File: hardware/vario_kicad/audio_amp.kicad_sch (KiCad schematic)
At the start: 14 parts

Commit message: update footprints, add LSE oscillator
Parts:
- R16, R17, R18, R19, R20, R21: footprint (none) -> Resistor_SMD:R_0402_1005Metric
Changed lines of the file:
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@@
 			)
 		)
-		(property "Footprint" ""
+		(property "Footprint" "Resistor_SMD:R_0402_1005Metric"
 			(at 194.31 81.788 90)
 			(effects
@@
 			)
 		)
-		(property "Footprint" ""
+		(property "Footprint" "Resistor_SMD:R_0402_1005Metric"
 			(at 220.98 95.758 90)
 			(effects
@@
 			)
 		)
-		(property "Footprint" ""
+		(property "Footprint" "Resistor_SMD:R_0402_1005Metric"
 			(at 110.49 76.708 90)
 			(effects
@@
 			)
 		)
-		(property "Footprint" ""
+		(property "Footprint" "Resistor_SMD:R_0402_1005Metric"
 			(at 194.31 95.758 90)
 			(effects
@@
 			)
 		)
-		(property "Footprint" ""
+		(property "Footprint" "Resistor_SMD:R_0402_1005Metric"
 			(at 162.56 103.378 90)
 			(effects
@@
 			)
 		)
-		(property "Footprint" ""
+		(property "Footprint" "Resistor_SMD:R_0402_1005Metric"
 			(at 162.56 89.408 90)
 			(effects

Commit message: start layout
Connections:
- net GND: now also U1.9 (GNDPAD)
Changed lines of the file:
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@@
+	)
+	(junction
+		(at 121.92 111.76)
+		(diameter 0)
+		(color 0 0 0 0)
 	)
 	(junction
@@
 	(wire
 		(pts
+			(xy 105.41 106.68) (xy 105.41 111.76)
+		)
+		(stroke
+			(width 0)
+			(type default)
+		)
+	)
+	(wire
+		(pts
 			(xy 64.77 77.47) (xy 64.77 74.93)
 		)
@@
 	(wire
 		(pts
+			(xy 105.41 111.76) (xy 121.92 111.76)
+		)
+		(stroke
+			(width 0)
+			(type default)
+		)
+	)
+	(wire
+		(pts
 			(xy 166.37 101.6) (xy 172.72 101.6)
 		)
@@
 	(wire
 		(pts
+			(xy 121.92 111.76) (xy 121.92 113.03)
+		)
+		(stroke
+			(width 0)
+			(type default)
+		)
+	)
+	(wire
+		(pts
 			(xy 118.11 100.33) (xy 121.92 100.33)
 		)
@@
 	(wire
 		(pts
-			(xy 121.92 110.49) (xy 121.92 113.03)
+			(xy 121.92 110.49) (xy 121.92 111.76)
 		)
 		(stroke
@@
 		(dnp no)
 		(property "Reference" "U1"
-			(at 106.68 81.28 0)
+			(at 111.76 83.82 0)
 			(effects
 				(font
@@
 		)
 		(property "Value" "~"
-			(at 106.68 83.82 0)
+			(at 111.76 83.82 0)
 			(effects
 				(font
@@
 		(pin "3"
 		)
+		(pin "9"
+		)
 		(instances

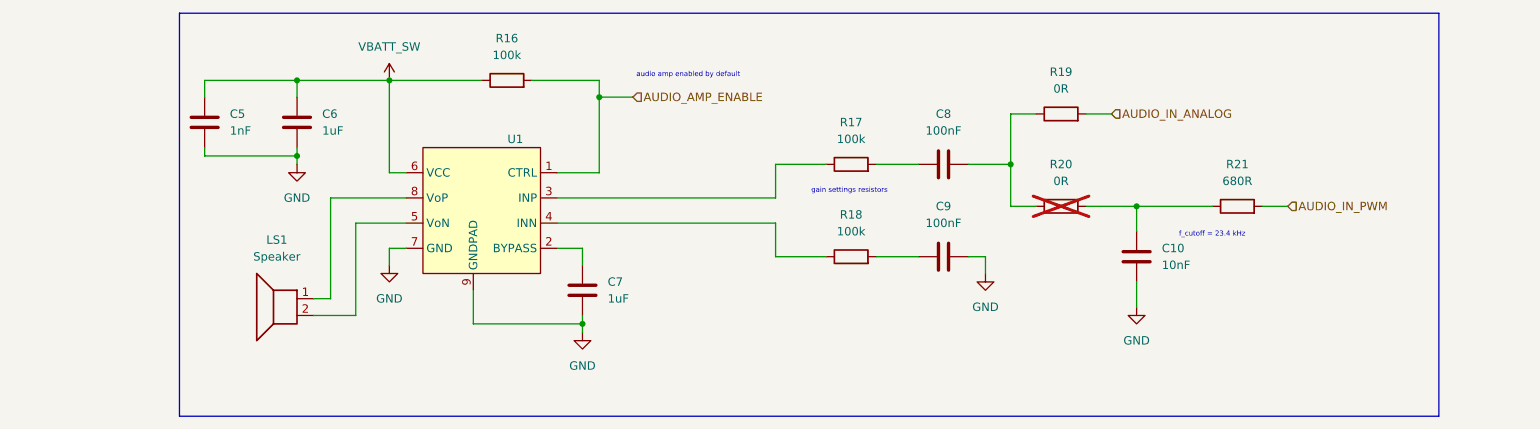
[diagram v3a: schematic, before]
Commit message: add test point to audio input
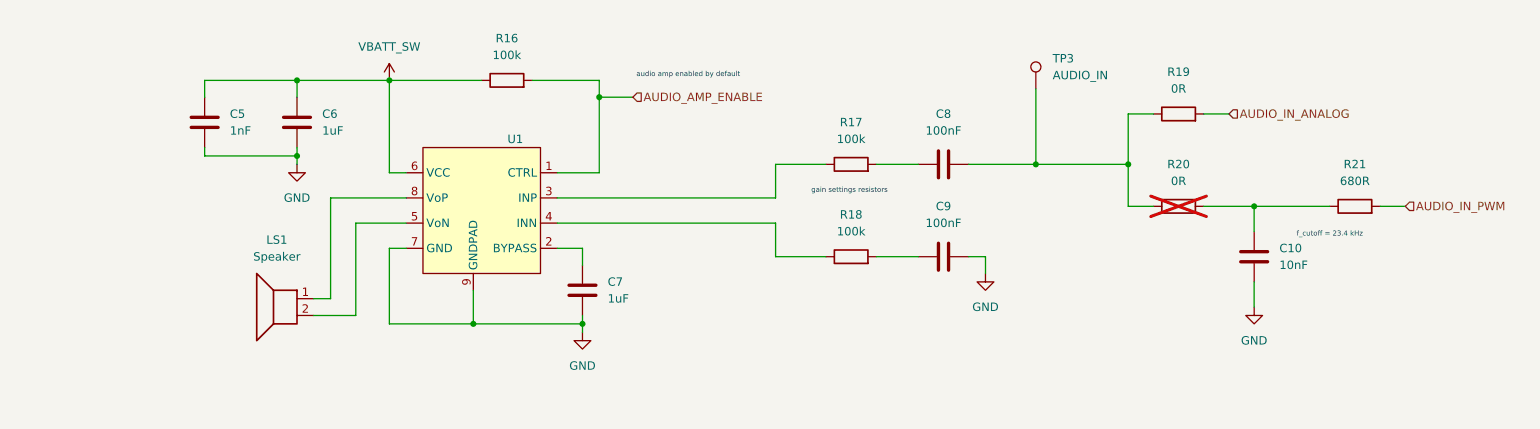
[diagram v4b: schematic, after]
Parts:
- added TP3: AUDIO_IN, symbol Connector:TestPoint
- U1: footprint Package_SO:MSOP-8-1EP_3x3mm_P0.65mm_EP1.73x1.85mm -> Package_SO:MSOP-8-1EP_3x3mm_P0.65mm_EP2.5x3mm_Mask1.73x2.36mm
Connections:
- net at C8.2, R19.1, R20.1: now also TP3.1
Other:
- moved on the sheet: C10, R19, R20, R21

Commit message: add footprints
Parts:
- TP3: footprint (none) -> TestPoint:TestPoint_Pad_D1.0mm
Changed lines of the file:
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@@
 			)
 		)
-		(property "Footprint" ""
+		(property "Footprint" "TestPoint:TestPoint_Pad_D1.0mm"
 			(at 195.58 76.2 0)
 			(effects

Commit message: minor changes
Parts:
- added TP5: TestPoint, symbol Connector:TestPoint
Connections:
- net AUDIO_IN_PWM: now also TP5.1
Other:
- moved on the sheet: C10, C5, C6, C7, C8, C9, LS1, R16, R17, R18, R19, R20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

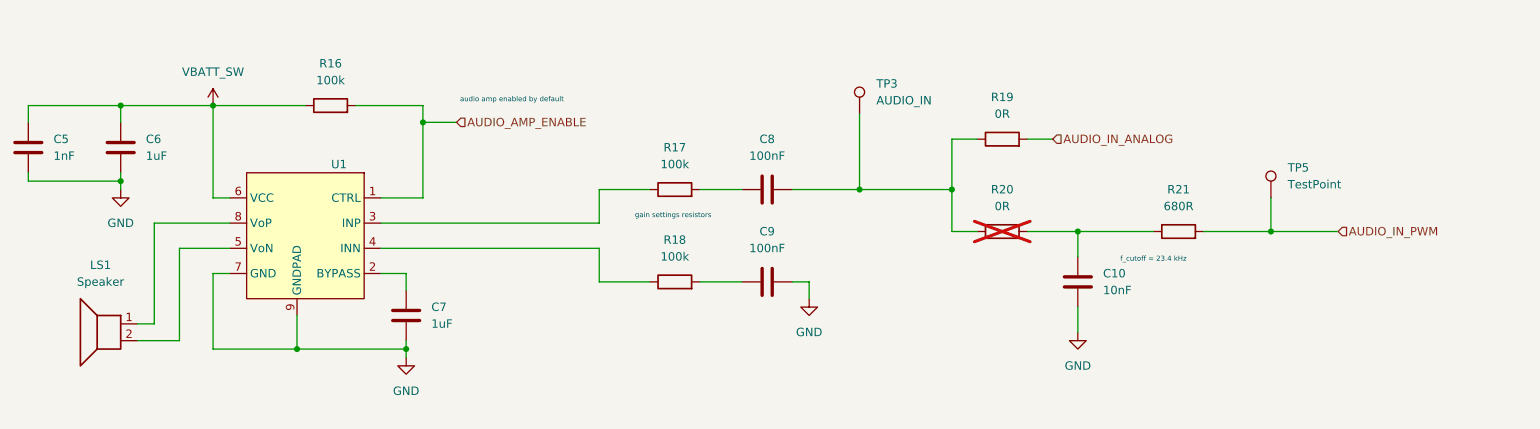
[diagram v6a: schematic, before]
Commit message: do not connect MCU to VBATT
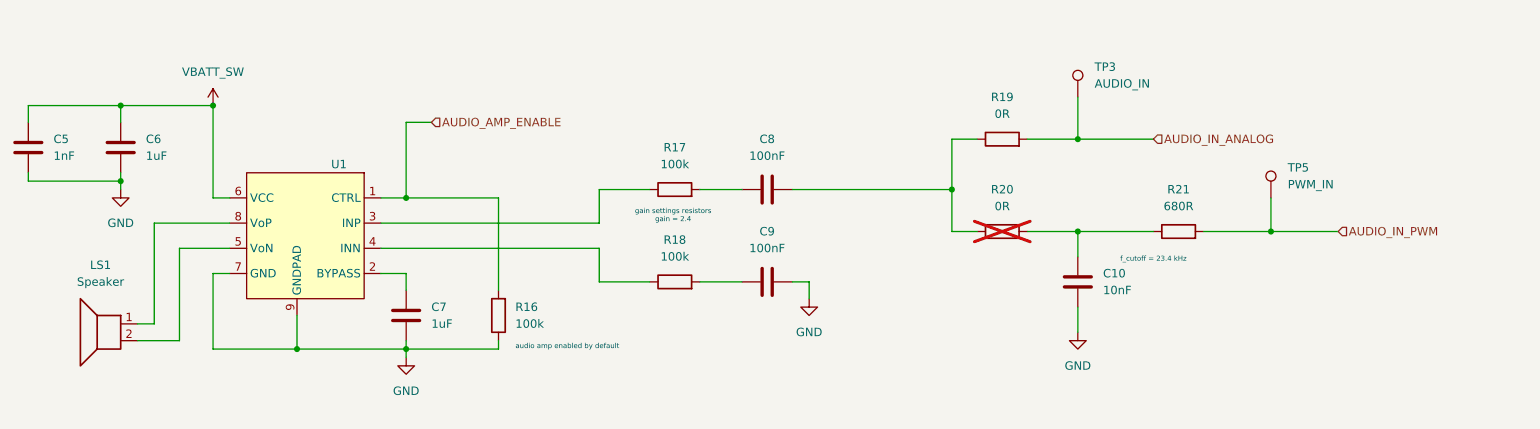
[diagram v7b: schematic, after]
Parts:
- TP5: value TestPoint -> PWM_IN
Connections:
- net AUDIO_IN_ANALOG: now also TP3.1
- net GND: now also R16.1
- net VBATT_SW: no longer R16.1
- net at C8.2, R19.1, R20.1: no longer TP3.1
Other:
- note added: "gain settings resistors gain = 2.4"
- note removed: "gain settings resistors"

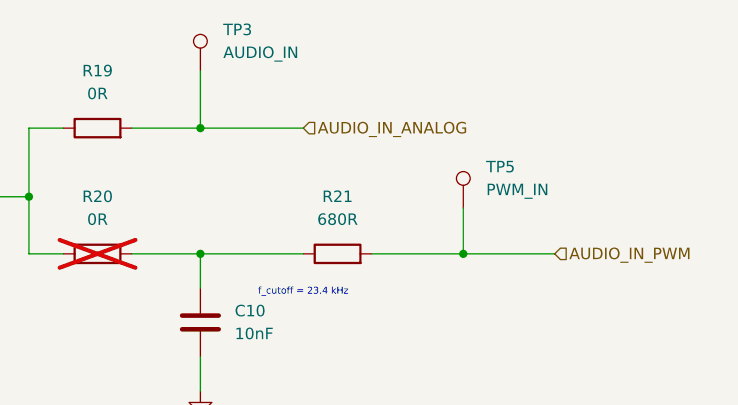
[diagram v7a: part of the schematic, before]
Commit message: add missing footprints
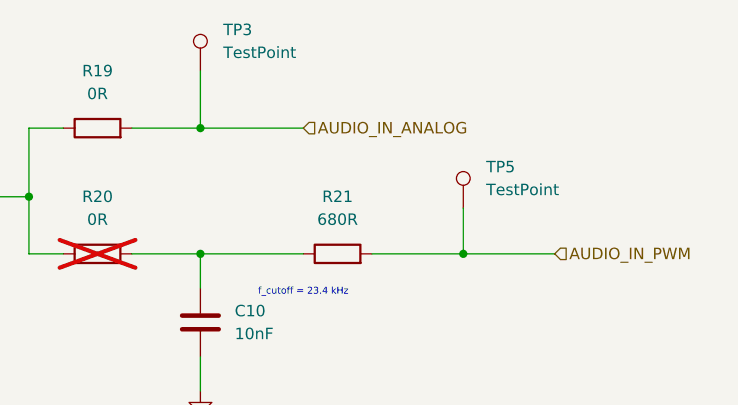
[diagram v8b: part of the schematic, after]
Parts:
- TP3: value AUDIO_IN -> TestPoint
- TP5: value PWM_IN -> TestPoint; footprint (none) -> TestPoint:TestPoint_Pad_D1.0mm
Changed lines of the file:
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@@
 			)
 		)
-		(property "Value" "PWM_IN"
+		(property "Value" "TestPoint"
 			(at 228.6 90.6779 0)
 			(effects
@@
 			)
 		)
-		(property "Footprint" ""
+		(property "Footprint" "TestPoint:TestPoint_Pad_D1.0mm"
 			(at 231.14 92.71 0)
 			(effects
@@
 			)
 		)
-		(property "Value" "AUDIO_IN"
+		(property "Value" "TestPoint"
 			(at 199.39 75.4379 0)
 			(effects
